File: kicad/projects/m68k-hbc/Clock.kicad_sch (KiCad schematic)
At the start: 13 parts, among them U15 DS1307+, U18 SN74LV1T34DBV, U20 SN74LV1T34DBV, U21 SN74LV1T34DBV, U35 Si5351A-B-GT, X5 10M, X5 4M, X5 70M, Y1 32.768k, Y3 25M

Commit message: Some Updates
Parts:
- removed C45, C46: 22p, Capacitor_SMD:C_1206_3216Metric_Pad1.33x1.80mm_HandSolder, symbol Device:C
- removed U18, U20, U21: SN74LV1T34DBV, Package_TO_SOT_SMD:SOT-23-5, symbol Logic_LevelTranslator:SN74LV1T34DBV
- removed U35: Si5351A-B-GT, Package_SO:MSOP-10_3x3mm_P0.5mm, symbol Oscillator:Si5351A-B-GT
- removed X5: 70M, Oscillator:Oscillator_SMD_SeikoEpson_SG8002CA-4Pin_7.0x5.0mm, symbol Oscillator:SG-8002CA
- removed X5: 10M, Oscillator:Oscillator_SMD_SeikoEpson_SG8002CA-4Pin_7.0x5.0mm, symbol Oscillator:SG-8002CA
- removed X5: 4M, Oscillator:Oscillator_SMD_SeikoEpson_SG8002CA-4Pin_7.0x5.0mm, symbol Oscillator:SG-8002CA
- removed Y3: 25M, Crystal:Crystal_HC52-6mm_Vertical, symbol Device:Crystal
- added C131: C, Capacitor_SMD:C_0603_1608Metric_Pad1.08x0.95mm_HandSolder, symbol Device:C
- added IC5, IC6, IC8, IC9: 551MLFT, Package_SO:SOIC-8_3.9x4.9mm_P1.27mm, symbol 551MLFT:551MLFT
- added IC7: 501MLFT, Package_SO:SOIC-8_3.9x4.9mm_P1.27mm, symbol 501MLFT:501MLFT
- added U29: MX8315MC, Package_SO:SOIC-14_3.9x8.7mm_P1.27mm, symbol m68k-hbc-ic:MX8315MC
- added U31: ICS542, Package_SO:SOIC-8_3.9x4.9mm_P1.27mm, symbol m68k-hbc-ic:ICS542
- added X5: SG-8002CA, Oscillator:Oscillator_SMD_SeikoEpson_SG8002CA-4Pin_7.0x5.0mm, symbol Oscillator:SG-8002CA
- R1: value 10k -> R; footprint Resistor_SMD:R_1206_3216Metric_Pad1.30x1.75mm_HandSolder -> Resistor_SMD:R_0603_1608Metric_Pad0.98x0.95mm_HandSolder
- Y1: value 32.768k -> Crystal
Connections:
- net +5V: now also IC5.7 (VDD), IC5.8 (OE), IC6.7 (VDD), IC6.8 (OE), IC7.2 (VDD), IC7.7 (OE), IC8.7 (VDD), IC8.8 (OE), IC9.7 (VDD), IC9.8 (OE), U29.9 (DVDD), U31.2 (VDD), U31.4 (S0), U31.6 (OE)
- net GND: now also C131.2, IC5.6 (GND), IC6.6 (GND), IC7.3 (GND), IC8.6 (GND), IC9.6 (GND), U29.7 (DGND), U31.3 (GND), U31.5 (S1)
- net REFRESH: no longer R1.2, U15.7 (SQW/OUT)
- new net: C131.1, U29.10 (CAP)
- new net: U29.3 (XI), X5.3 (OUT)
- new net +5VA: U29.14 (AVDD)
- new net CFG_CLK0: U29.13 (S2)
- new net CFG_CLK1: U29.12 (S1)
- new net CFG_CLK2: U29.11 (S0)
- new net CLK_24M: IC8.5 (Q4)
- new net CLK_2M: U31.7 (CLK/2)
- new net CLK_8M: IC7.5 (CLK), IC9.1 (ICLK), IC9.5 (Q4)
- new net CLK_CDC: IC5.4 (Q3)
- new net CLK_CPU: IC5.2 (Q1)
- new net CLK_DIV24M: IC8.4 (Q3), U31.1 (ICLK)
- new net CLK_DIV4M: IC7.1 (X1/ICLK), U31.8 (CLK)
- new net CLK_FPU: IC5.3 (Q2)
- new net CLK_ISA: IC9.2 (Q1)
- new net CLK_ISAOSC: IC6.2 (Q1)
- new net CLK_LOCAL: IC5.5 (Q4)
- new net CLK_PEP: IC8.3 (Q2)
- new net CLK_PER: IC8.1 (ICLK), U29.5 (PCK)
- new net CLK_REF: IC6.1 (ICLK), IC6.5 (Q4), U29.4 (XCK)
- new net CLK_SBC: IC8.2 (Q1)
- new net CLK_VAR: IC5.1 (ICLK), U29.8 (CK)
- new net GNDA: U29.1 (AGND)
- new net RTCCLK: R1.2, U15.7 (SQW/OUT)
- new net ~{CLK_LOP}: U29.6 (~{LOP})
- no-connect marks 0 -> 4
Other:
- note added: "System Serial Bus"
- note added: "VARCLK: Configurable {20, 25, 33.33, 40, 50, 60, 66,67, 80}MHz 24MCLK: 24MHz REFCLK: 14.31818MHz"

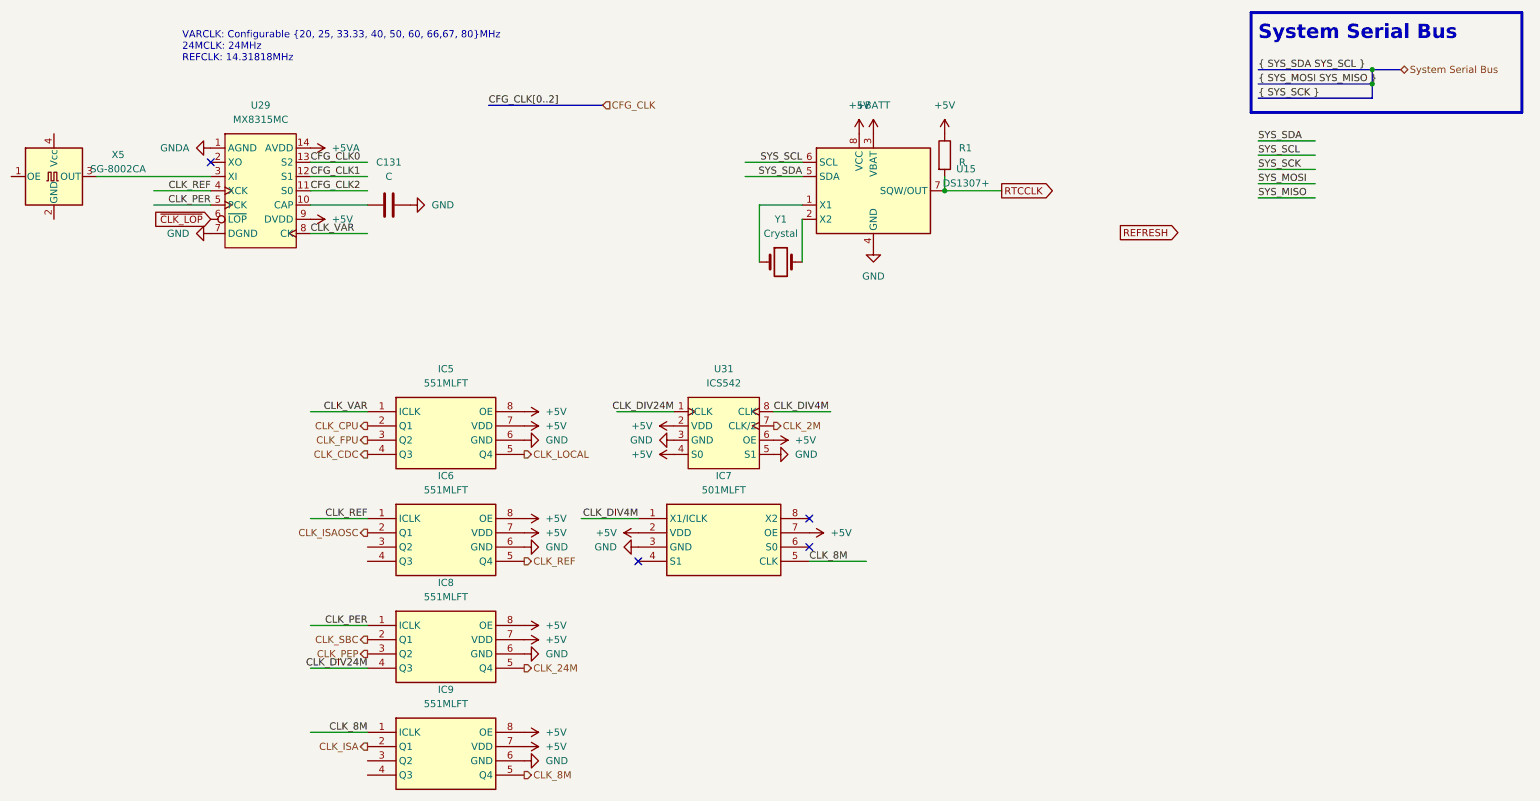
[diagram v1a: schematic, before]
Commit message: Large changes: EHBCSimpleEmu, kicad, fwcode, docs
This commit contains some large changes:
- Removed EHBCSimpleEmu (Moved to kms1212/llemu, kms1212/qemu)
- (likely) Removed fwcode; now it only boots and stops
- Modified documents
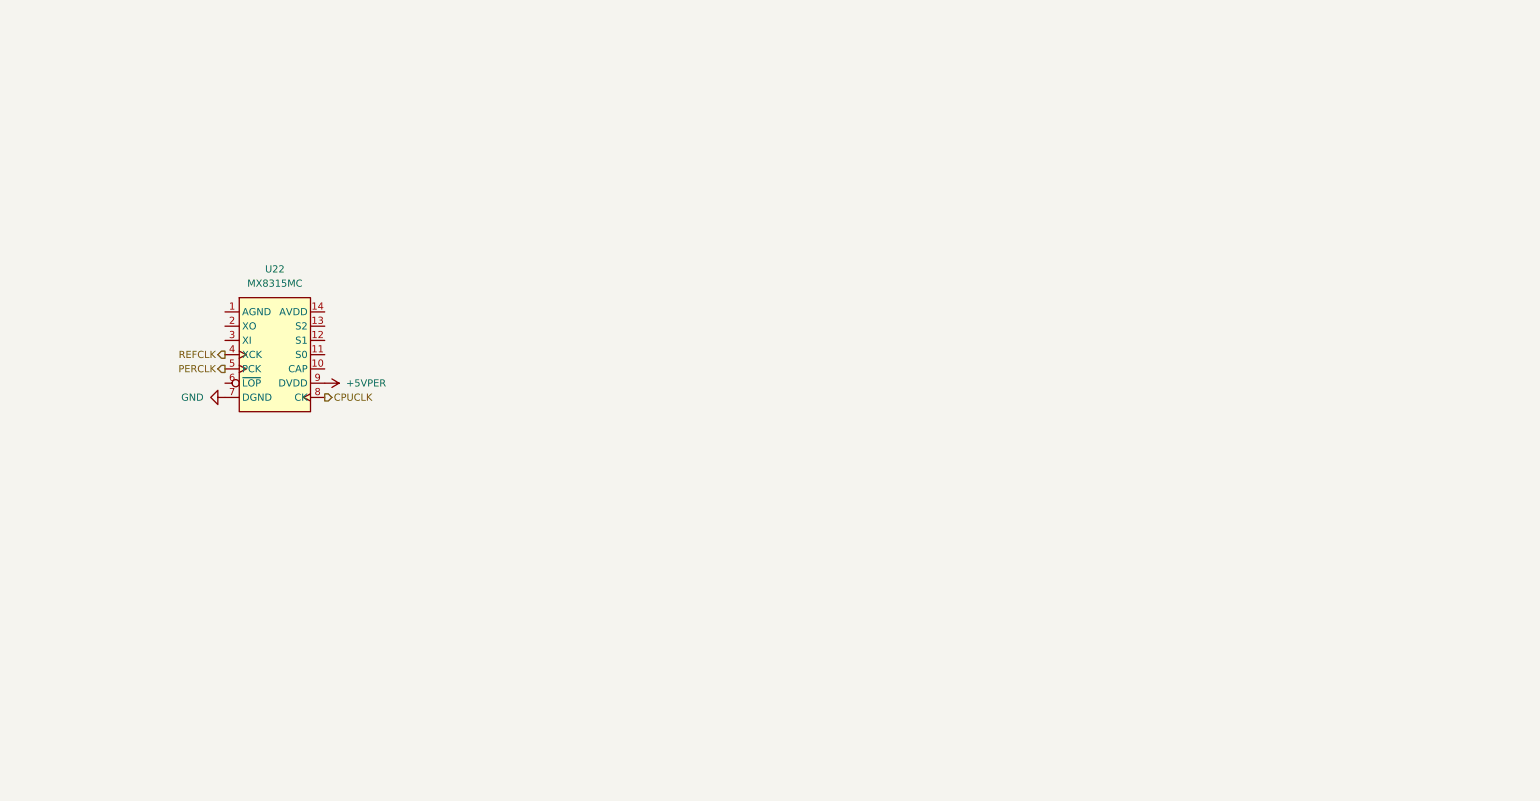
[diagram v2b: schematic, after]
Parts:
- removed C131: C, Capacitor_SMD:C_0603_1608Metric_Pad1.08x0.95mm_HandSolder, symbol Device:C
- removed IC5, IC6, IC8, IC9: 551MLFT, Package_SO:SOIC-8_3.9x4.9mm_P1.27mm, symbol 551MLFT:551MLFT
- removed IC7: 501MLFT, Package_SO:SOIC-8_3.9x4.9mm_P1.27mm, symbol 501MLFT:501MLFT
- removed R1: R, Resistor_SMD:R_0603_1608Metric_Pad0.98x0.95mm_HandSolder, symbol Device:R
- removed U15: DS1307+, Package_DIP:DIP-8_W7.62mm, symbol Timer_RTC:DS1307+
- removed U29: MX8315MC, Package_SO:SOIC-14_3.9x8.7mm_P1.27mm, symbol m68k-hbc-ic:MX8315MC
- removed U31: ICS542, Package_SO:SOIC-8_3.9x4.9mm_P1.27mm, symbol m68k-hbc-ic:ICS542
- removed X5: SG-8002CA, Oscillator:Oscillator_SMD_SeikoEpson_SG8002CA-4Pin_7.0x5.0mm, symbol Oscillator:SG-8002CA
- removed Y1: Crystal, Crystal:Crystal_Round_D2.0mm_Vertical, symbol Device:Crystal
- added U22: MX8315MC, Package_SO:SOIC-14_3.9x8.7mm_P1.27mm, symbol m68k-hbc-ic:MX8315MC
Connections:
- net GND: now also U22.7 (DGND)
- new net +5VPER: U22.9 (DVDD)
- new net CPUCLK: U22.8 (CK)
- new net PERCLK: U22.5 (PCK)
- new net REFCLK: U22.4 (XCK)
- no-connect marks 4 -> 0
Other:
- note removed: "System Serial Bus"
- note removed: "VARCLK: Configurable {20, 25, 33.33, 40, 50, 60, 66,67, 80}MHz 24MCLK: 24MHz REFCLK: 14.31818MHz"
